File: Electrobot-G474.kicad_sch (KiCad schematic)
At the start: 72 parts, among them J1 Conn_01x03, J10 Conn_01x03, J11 Conn_01x04, J12 Conn_01x04, J13 Conn_01x04, J14 Conn_01x04, J15 Conn_01x04, J16 Conn_01x04, J17 Conn_01x03, J18 Conn_01x03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

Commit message: Mise à jour du schéma et routage de la carte
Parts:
- added JP1: SolderJumper_3_Open, Connector_PinHeader_2.54mm:PinHeader_1x03_P2.54mm_Vertical, symbol Jumper:SolderJumper_3_Open
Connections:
- net +6.5V: now also JP1.1 (A)
- net Cde_Mosfet: now also U3.CN7_21 (PB7); no longer U3.CN7_7 (PB8-BOOT0)
- net Codeur1_B: now also U3.CN10_12 (PA12); no longer U3.CN7_21 (PB7)
- net Etor2: now also U3.CN10_2 (PC8); no longer U3.CN10_3 (PB8)
- net LED1: now also U3.CN10_24 (PB1); no longer U3.CN10_35 (PA2/PC4)
- net LED2: now also U3.CN10_22 (PB2); no longer U3.CN10_37 (PA3/PC5)
- net Mot1_Sens1: now also U3.CN10_17 (PB6); no longer U3.CN10_15 (PA7)
- net Mot1_Sens2: now also U3.CN10_15 (PA7); no longer U3.CN10_17 (PB6)
- net Mot3_Sens1: now also U3.CN7_37 (PC3); no longer U3.CN7_35 (PC2)
- net Mot3_Sens2: now also U3.CN7_35 (PC2); no longer U3.CN7_37 (PC3)
- net Servo1_PWM: now also J25.1 (Pin_1), U3.CN10_18 (PB11); no longer J17.1 (Pin_1), U3.CN7_30 (PA1)
- net Servo2_PWM: now also J17.1 (Pin_1); no longer J24.1 (Pin_1)
- net Servo3_PWM: now also J24.1 (Pin_1), U3.CN7_30 (PA1); no longer J18.1 (Pin_1), U3.CN10_25 (PB10)
- net Servo4_PWM: now also J18.1 (Pin_1), U3.CN10_25 (PB10); no longer J25.1 (Pin_1), U3.CN10_18 (PB11)
- net VBAT: now also JP1.3 (B); no longer J3.2 (+)
- net DRAIN: now reaches J3.1 (-), Q1.2 (D), R1.1
- new net +Vmosfet: J3.2 (+), JP1.2 (C)
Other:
- note added: "Choix de la tension de sortie MOSFET"
- note added: "RS: 193-9786 Farnell: 3132424 Mouser: 511-NUCLEO-G474RE Digikey: 497-19491-ND"
- note added: "RX/TX STLINK"
- title: (none) -> Electrobot G474
- moved on the sheet: J17, J18, J24, J25

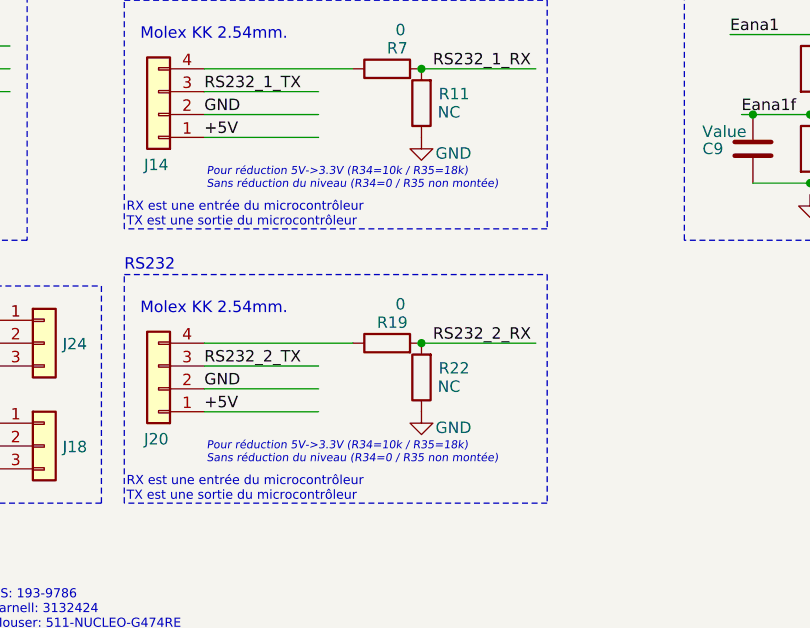
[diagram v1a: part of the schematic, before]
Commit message: Correction des annotations du schéma sur la division de tension des RX RS232
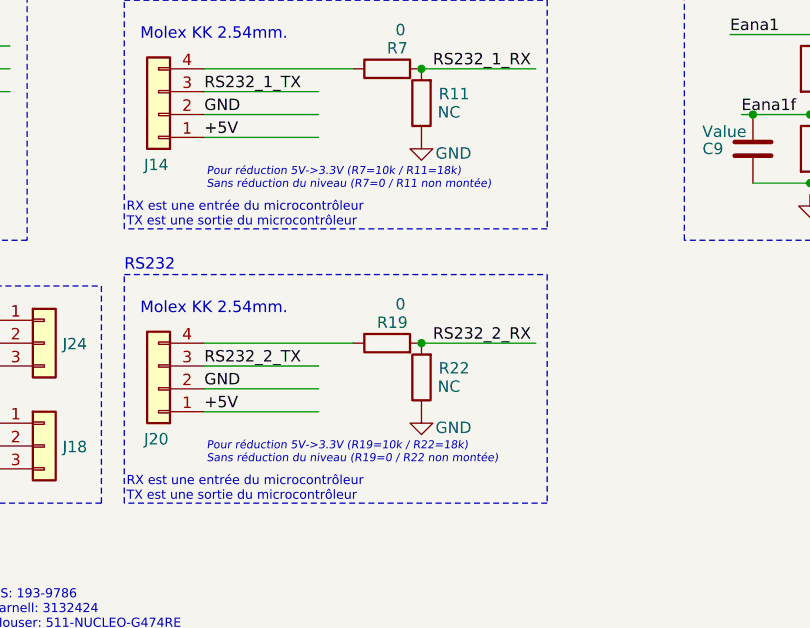
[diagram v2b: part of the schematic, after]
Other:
- note added: "Pour réduction 5V->3.3V (R19=10k / R22=18k) Sans réduction du niveau (R19=0 / R22 non montée)"
- note added: "Pour réduction 5V->3.3V (R7=10k / R11=18k) Sans réduction du niveau (R7=0 / R11 non montée)"
- note removed: "Pour réduction 5V->3.3V (R34=10k / R35=18k) Sans réduction du niveau (R34=0 / R35 non montée)"
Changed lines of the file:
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@@
 	(title_block
 		(title "Electrobot G474")
-		(rev "V1.0")
+		(rev "V1.1")
 	)
 	(junction
@@
 		)
 	)
-	(text "Pour réduction 5V->3.3V (R34=10k / R35=18k)\nSans réduction du niveau (R34=0 / R35 non montée)\n\n"
+	(text "Pour réduction 5V->3.3V (R19=10k / R22=18k)\nSans réduction du niveau (R19=0 / R22 non montée)\n\n"
 		(exclude_from_sim no)
 		(at 82.804 120.904 0)
@@
 		)
 	)
-	(text "Pour réduction 5V->3.3V (R34=10k / R35=18k)\nSans réduction du niveau (R34=0 / R35 non montée)\n\n"
+	(text "Pour réduction 5V->3.3V (R7=10k / R11=18k)\nSans réduction du niveau (R7=0 / R11 non montée)\n\n"
 		(exclude_from_sim no)
 		(at 82.804 90.424 0)
